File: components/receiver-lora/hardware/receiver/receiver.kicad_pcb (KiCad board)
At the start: 2 copper layers, 60 x 98 mm, 4 parts, among them J1 Conn_Coaxial_Small, U1 GY-NEO6MV2, U2 ESP32-S3-DEVKITC-1-N8R8, U3 RFM95W-915S2

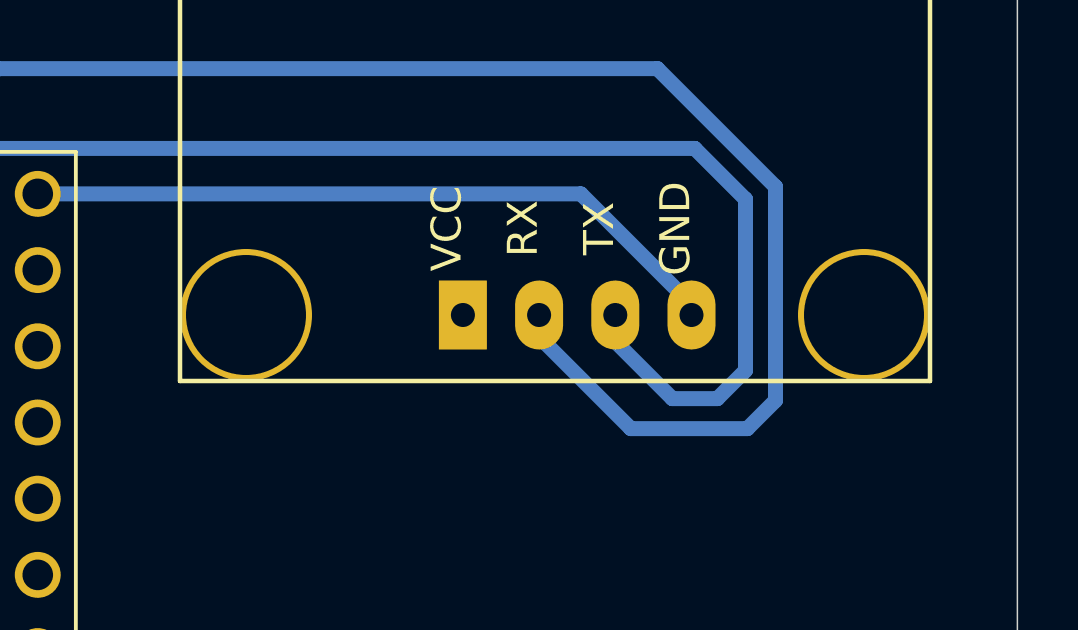
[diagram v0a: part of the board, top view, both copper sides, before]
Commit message: Update on receiver PCB (still need modifications)
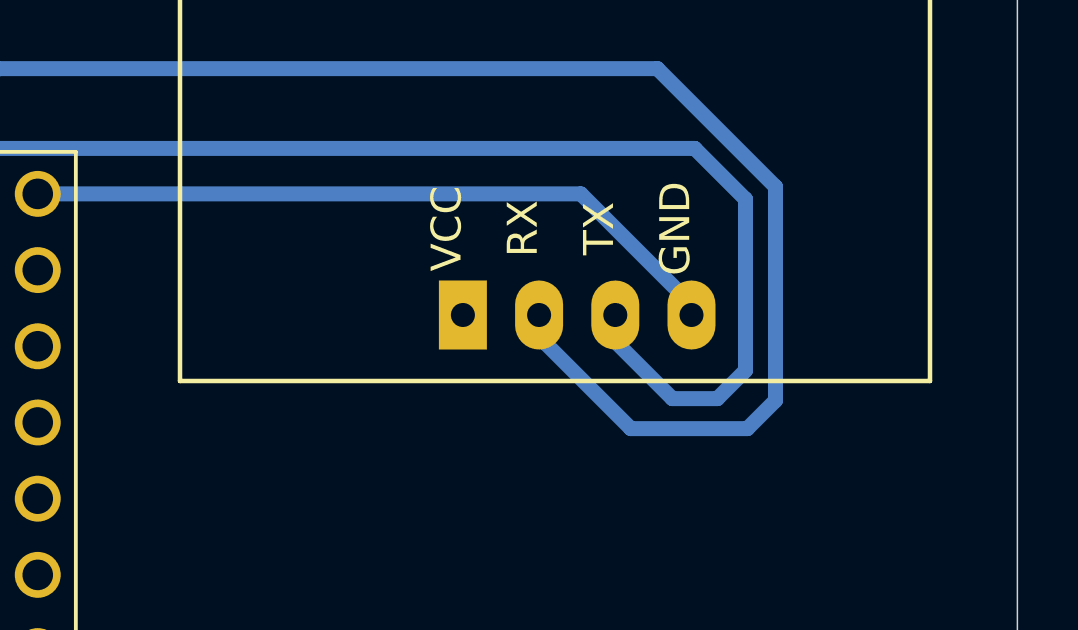
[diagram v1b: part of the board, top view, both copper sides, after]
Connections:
- U2 pad J1_22: Net-(J1-Ext) -> unconnected-(U2-GND-PadJ1_22)
- U2 pad J3_21: Net-(J1-Ext) -> unconnected-(U2-GND-PadJ3_21)
- U2 pad J3_22: Net-(J1-Ext) -> unconnected-(U2-GND-PadJ3_22)

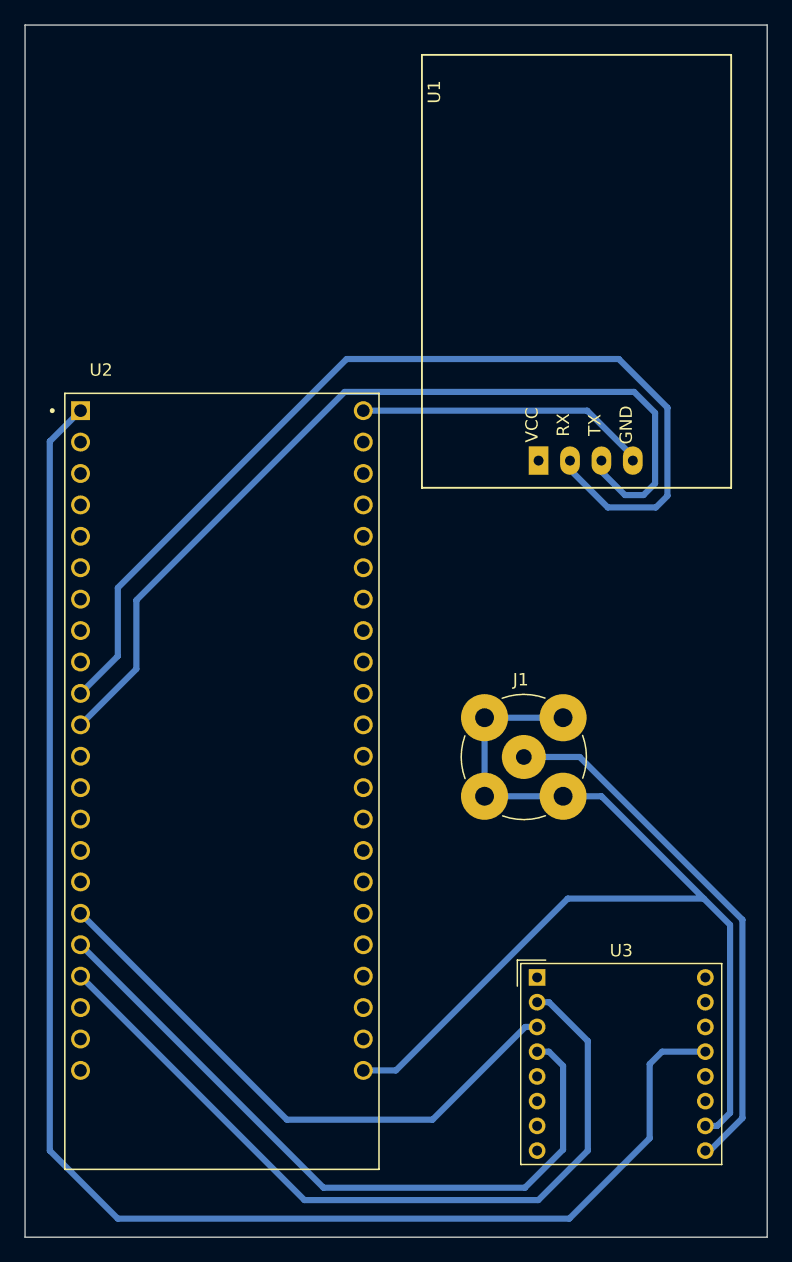
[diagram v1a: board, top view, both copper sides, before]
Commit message: Update on esp32 dimensions
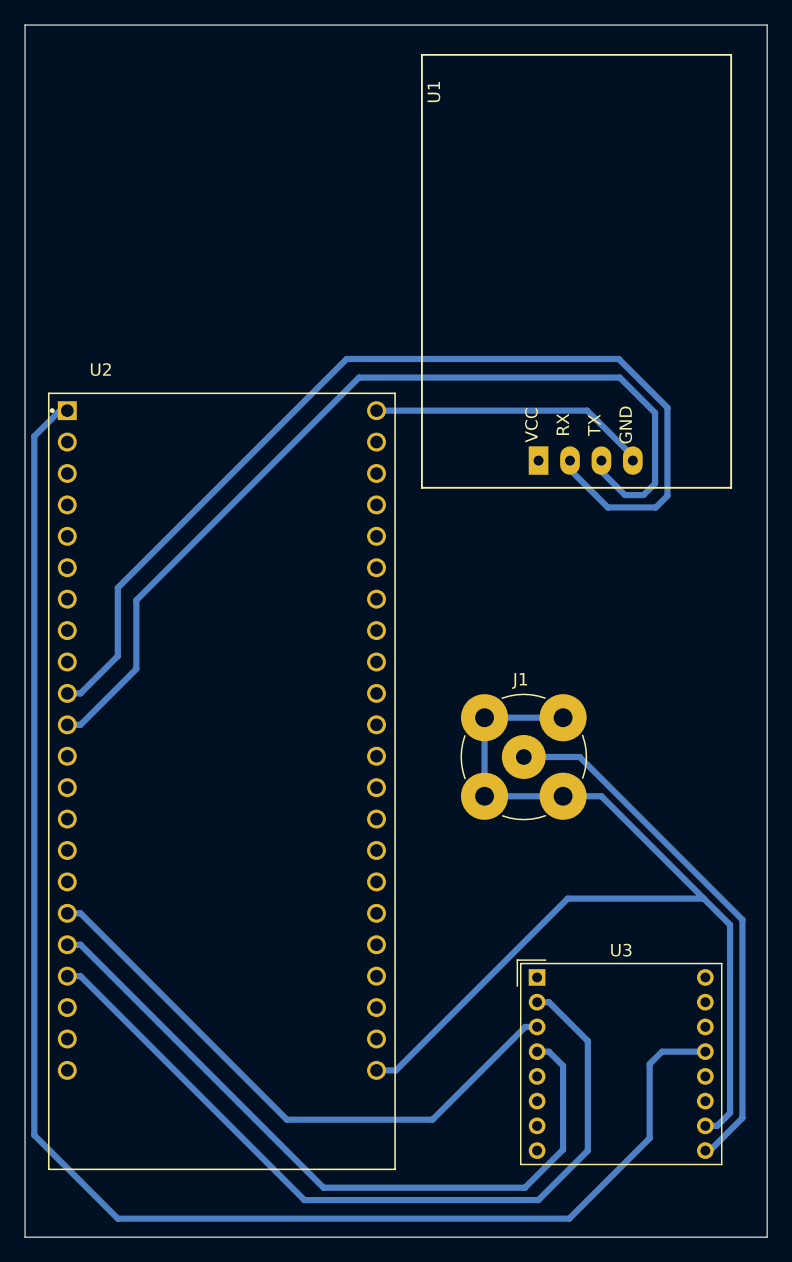
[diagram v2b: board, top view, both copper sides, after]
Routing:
- net Net-(J1-Ext): track 111.4 -> 109.2 mm
- net Net-(U1-TX): track 73.7 -> 75.7 mm
- net Net-(U1-RX): track 80.9 -> 82.0 mm
- net /SPI_SCK: track 57.8 -> 58.8 mm
- net /SPI_MOSI: track 46.9 -> 48.0 mm
- net /SPI_MISO: track 64.4 -> 65.5 mm
- net Net-(U3-3.3V): track 125.2 -> 126.2 mm
